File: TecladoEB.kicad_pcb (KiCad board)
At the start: 2 copper layers, 48.4 x 46.3 mm, 18 parts, among them J1 GND-SIG

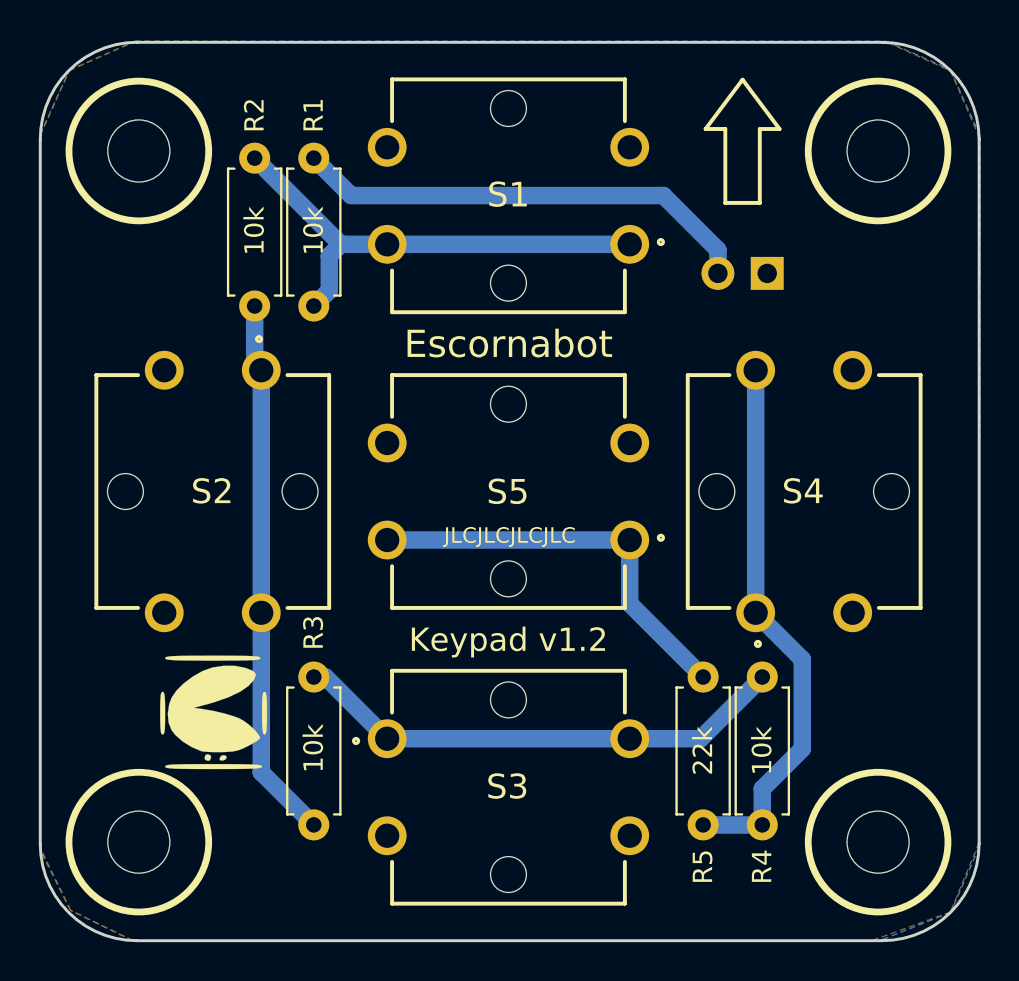
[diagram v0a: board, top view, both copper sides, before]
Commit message: Updated to v1.3, including new LICENSE
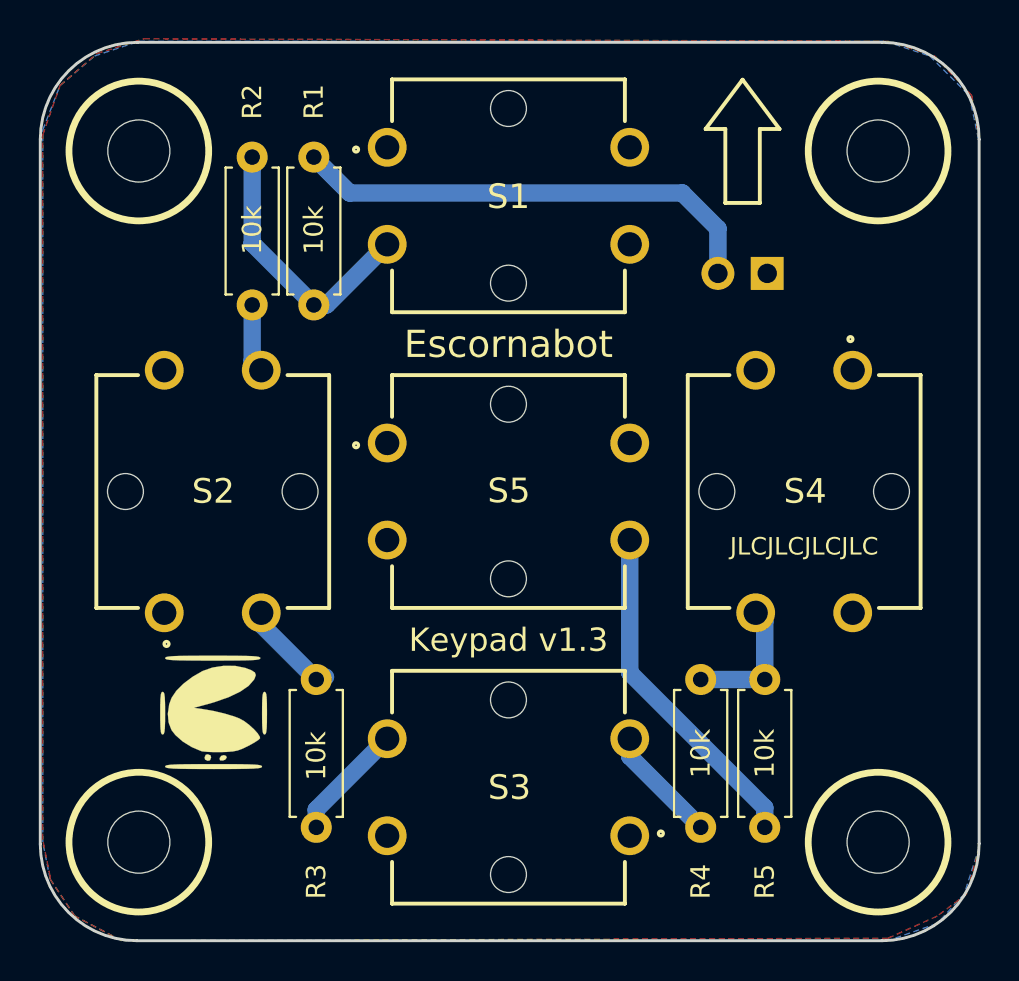
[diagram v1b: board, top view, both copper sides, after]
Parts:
- J1: value GND-SIG -> GND SIG
- R1, R2, R3, R4: footprint Resistor_THT:R_Axial_DIN0207_L6.3mm_D2.5mm_P7.62mm_Horizontal -> Components:R_Axial_DIN0207_L6.3mm_D2.5mm_P7.62mm_Horizontal_10k
- R5: value 22k -> 10k; footprint Resistor_THT:R_Axial_DIN0207_L6.3mm_D2.5mm_P7.62mm_Horizontal -> Components:R_Axial_DIN0207_L6.3mm_D2.5mm_P7.62mm_Horizontal_10k
- S1, S2, S3, S4, S5: footprint Components:EB-B3F-4055 -> Components:B3F-4050
- moved R5 8.37 mm to (137.3, 140.5), turned to 90 degrees
- moved R4 8.14 mm to (134.0, 132.8), turned to 270 degrees
- moved R3 7.75 mm to (114.2, 140.5), turned to 90 degrees
- moved R2 0.14 mm to (110.9, 113.5)
- moved R1 0.05 mm to (114.1, 113.5)
- turned S1 to 180 degrees
- turned S2 to 270 degrees
- turned S3 to 0 degrees
- turned S4 to 90 degrees
- turned S5 to 180 degrees
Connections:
- S1 pad 1: Net-(R1-Pad1) -> GND
- S1 pad 2: Net-(R1-Pad1) -> GND
- S1 pad 3: GND -> Net-(R1-Pad1)
- S1 pad 4: GND -> Net-(R1-Pad1)
- S2 pad 1: Net-(R2-Pad1) -> GND
- S2 pad 2: Net-(R2-Pad1) -> GND
- S2 pad 3: GND -> Net-(R2-Pad1)
- S2 pad 4: GND -> Net-(R2-Pad1)
- S3 pad 1: Net-(R3-Pad1) -> GND
- S3 pad 2: Net-(R3-Pad1) -> GND
- S3 pad 3: GND -> Net-(R3-Pad1)
- S3 pad 4: GND -> Net-(R3-Pad1)
- S4 pad 1: Net-(R4-Pad1) -> GND
- S4 pad 2: Net-(R4-Pad1) -> GND
- S4 pad 3: GND -> Net-(R4-Pad1)
- S4 pad 4: GND -> Net-(R4-Pad1)
- S5 pad 1: Net-(R5-Pad1) -> GND
- S5 pad 2: Net-(R5-Pad1) -> GND
- S5 pad 3: GND -> Net-(R5-Pad1)
- S5 pad 4: GND -> Net-(R5-Pad1)
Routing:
- net Net-(R4-Pad1): track 28.3 -> 6.93 mm
- net Net-(R2-Pad1): track 28.0 -> 9.26 mm
- net Net-(R3-Pad1): track 25.7 -> 12.2 mm
- net Net-(R1-Pad1): track 24.9 -> 14.0 mm
- net Net-(R5-Pad1): track 21.1 -> 17.7 mm
- net Net-(J1-Pad2): track 24.0 -> 24.7 mm
- added copper zone on B.Cu, net GND
- removed copper zone on B.Cu, net (none)
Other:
- board text added: "Keypad v1.3"
- board text removed: "Keypad v1.2"

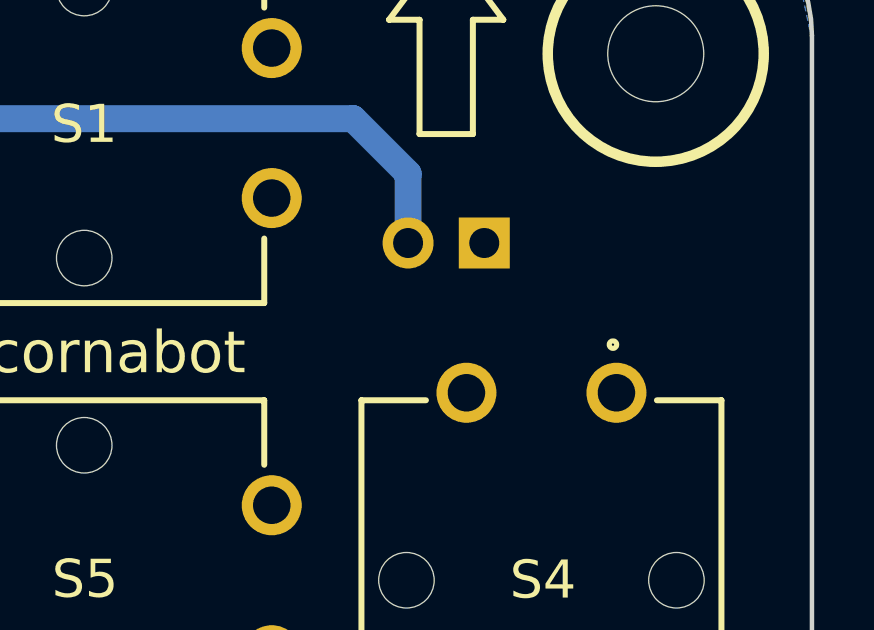
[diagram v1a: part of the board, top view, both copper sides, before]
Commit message: v1.3 Make KiCadStepUp happy and minor cosmetic changes
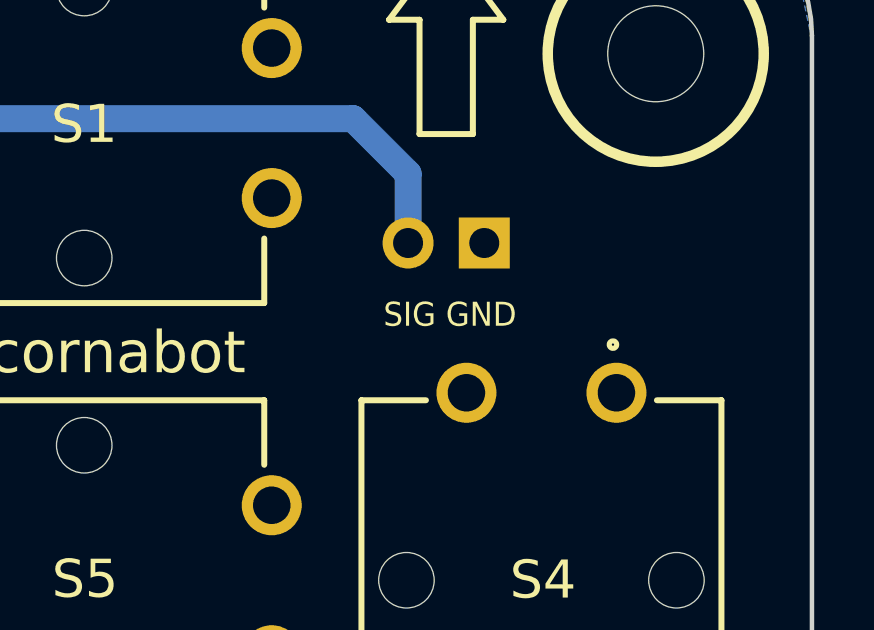
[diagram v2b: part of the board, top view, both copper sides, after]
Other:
- rule pad_to_mask_clearance: 0.2 -> 0
- board text added: "SIG GND"
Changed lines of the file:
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@@
   (general
     (thickness 1.6)
-    (drawings 24)
+    (drawings 25)
     (tracks 24)
     (zones 0)
@@
     (pad_size 3.200001 3.200001)
     (pad_drill 3.200001)
-    (pad_to_mask_clearance 0.2)
+    (pad_to_mask_clearance 0)
     (aux_axis_origin 100 146.3)
     (grid_origin 100 146.3)
@@
     (descr "Resistor, Axial_DIN0207 series, Axial, Horizontal, pin pitch=7.62mm, 0.25W = 1/4W, length*diameter=6.3*2.5mm^2, http://cdn-reichelt.de/documents/datenblatt/B400/1_4W%23YAG.pdf")
     (tags "Resistor Axial_DIN0207 series Axial Horizontal pin pitch 7.62mm 0.25W = 1/4W length 6.3mm diameter 2.5mm")
-    (fp_text reference R4 (at 10.414 0 90) (layer F.SilkS)
-      (effects (font (size 1 1) (thickness 0.15)))
-    )
-    (fp_text value 10k (at 3.81 0 90) (layer F.SilkS)
-      (effects (font (size 1 1) (thickness 0.15)))
-    )
-    (fp_text user %R (at -2.794 0 90) (layer F.Fab)
+    (fp_text reference R4 (at 10.414 0 270) (layer F.SilkS)
+      (effects (font (size 1 1) (thickness 0.15)))
+    )
+    (fp_text value 10k (at 3.81 0 270) (layer F.SilkS)
       (effects (font (size 1 1) (thickness 0.15)))
     )
@@
     (fp_line (start 0.66 1.25) (end 6.96 1.25) (layer F.Fab) (width 0.1))
     (fp_line (start 0.66 -1.25) (end 0.66 1.25) (layer F.Fab) (width 0.1))
+    (fp_text user %R (at -2.794 0 270) (layer F.Fab)
+      (effects (font (size 1 1) (thickness 0.15)))
+    )
     (pad 1 thru_hole circle (at 0 0 270) (size 1.6 1.6) (drill 0.8) (layers *.Cu *.Mask)
       (net 5 "Net-(R4-Pad1)"))
@@
       (offset (xyz 3.81 0 1.25))
       (scale (xyz 1 1 1))
-      (rotate (xyz 0 0 0))
+      (rotate (xyz 0 0 180))
     )
   )
@@
     )
     (fp_text value 10k (at 3.81 0 270) (layer F.SilkS)
-      (effects (font (size 1 1) (thickness 0.15)))
-    )
-    (fp_text user %R (at 10.414 0 270) (layer F.Fab)
       (effects (font (size 1 1) (thickness 0.15)))
     )
@@
     (fp_line (start 0.66 1.25) (end 6.96 1.25) (layer F.Fab) (width 0.1))
     (fp_line (start 0.66 -1.25) (end 0.66 1.25) (layer F.Fab) (width 0.1))
+    (fp_text user %R (at 10.414 0 270) (layer F.Fab)
+      (effects (font (size 1 1) (thickness 0.15)))
+    )
     (pad 1 thru_hole circle (at 0 0 90) (size 1.6 1.6) (drill 0.8) (layers *.Cu *.Mask)
       (net 6 "Net-(R5-Pad1)"))
@@
     )
     (fp_text value 10k (at 3.683 0 270) (layer F.SilkS)
-      (effects (font (size 1 1) (thickness 0.15)))
-    )
-    (fp_text user %R (at 10.414 0 270) (layer F.Fab)
       (effects (font (size 1 1) (thickness 0.15)))
     )
@@
     (fp_line (start 0.66 1.25) (end 6.96 1.25) (layer F.Fab) (width 0.1))
     (fp_line (start 0.66 -1.25) (end 0.66 1.25) (layer F.Fab) (width 0.1))
+    (fp_text user %R (at 10.414 0 270) (layer F.Fab)
+      (effects (font (size 1 1) (thickness 0.15)))
+    )
     (pad 1 thru_hole circle (at 0 0 90) (size 1.6 1.6) (drill 0.8) (layers *.Cu *.Mask)
       (net 4 "Net-(R3-Pad1)"))
@@
     )
     (fp_text value 10k (at 3.865 0 90) (layer F.SilkS)
-      (effects (font (size 1 1) (thickness 0.15)))
-    )
-    (fp_text user %R (at 10.469 0 90) (layer F.Fab)
       (effects (font (size 1 1) (thickness 0.15)))
     )
@@
     (fp_line (start 0.66 1.25) (end 6.96 1.25) (layer F.Fab) (width 0.1))
     (fp_line (start 0.66 -1.25) (end 0.66 1.25) (layer F.Fab) (width 0.1))
+    (fp_text user %R (at 10.469 0 90) (layer F.Fab)
+      (effects (font (size 1 1) (thickness 0.15)))
+    )
     (pad 1 thru_hole circle (at 0 0 90) (size 1.6 1.6) (drill 0.8) (layers *.Cu *.Mask)
       (net 2 "Net-(R2-Pad1)"))
@@
     )
     (fp_text value 10k (at 3.865 0 90) (layer F.SilkS)
-      (effects (font (size 1 1) (thickness 0.15)))
-    )
-    (fp_text user %R (at 10.469 0 90) (layer F.Fab)
       (effects (font (size 1 1) (thickness 0.15)))
     )
@@
     (fp_line (start 0.66 1.25) (end 6.96 1.25) (layer F.Fab) (width 0.1))
     (fp_line (start 0.66 -1.25) (end 0.66 1.25) (layer F.Fab) (width 0.1))
+    (fp_text user %R (at 10.469 0 90) (layer F.Fab)
+      (effects (font (size 1 1) (thickness 0.15)))
+    )
     (pad 1 thru_hole circle (at 0 0 90) (size 1.6 1.6) (drill 0.8) (layers *.Cu *.Mask)
       (net 1 "Net-(R1-Pad1)"))
@@
       (xy -0.632646 2.895785) (xy -0.576777 3.302) (xy 0.576777 3.302) (xy 0.632646 2.895785)) (layer B.SilkS) (width 0.01))
   )
+  (gr_text "SIG GND" (at 136.322 114.296) (layer F.SilkS)
+    (effects (font (size 0.8 0.75) (thickness 0.15)))
+  )
   (gr_text Escornabot (at 124.13 115.566) (layer F.SilkS)

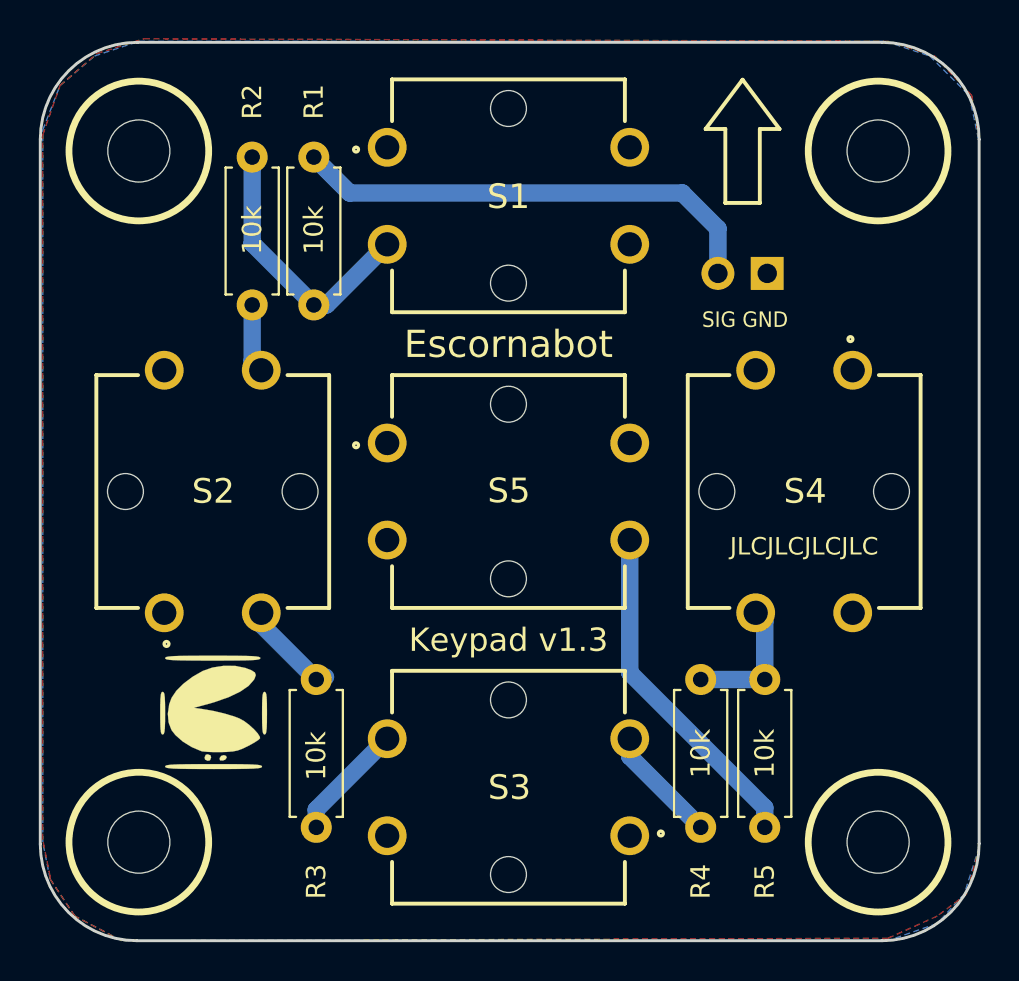
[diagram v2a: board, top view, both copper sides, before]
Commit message: Updated to v1.4 with bigger pads
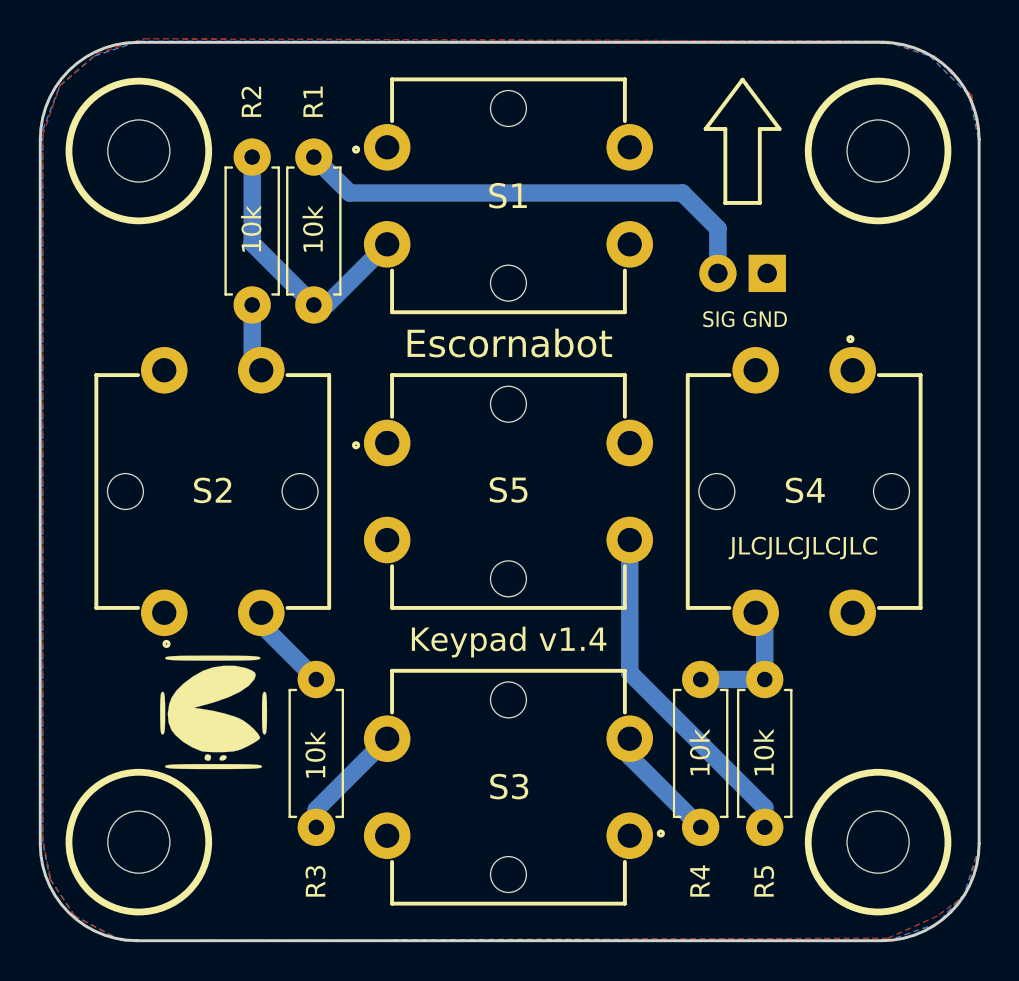
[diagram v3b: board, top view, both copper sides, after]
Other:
- board text added: "Keypad v1.4"
- board text removed: "Keypad v1.3"
